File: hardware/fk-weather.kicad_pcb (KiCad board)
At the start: 2 copper layers, 28.7 x 107.4 mm, 78 parts, among them J1 MICRO-USB, J2 CONN_01X03, J6 CONN-HDR-2x5, M1 MOUNT_HOLE, M2 MOUNT_HOLE, M3 MOUNT_HOLE, M4 MOUNT_HOLE, P101 CONN_01X05, Q1 2N7002LT1G, Q2 2N7002LT1G, Q3 2N7002LT1G, SW1 SPNO, U1 ATSAMD21G18A-AU, U101 TSL2591, U102 MPL3115A2, U103 BNO055, U104 SHT31, U2 MCP1700T-XXX2E, U3 MAX4466, Y1 FC-135, Y101 FC-135

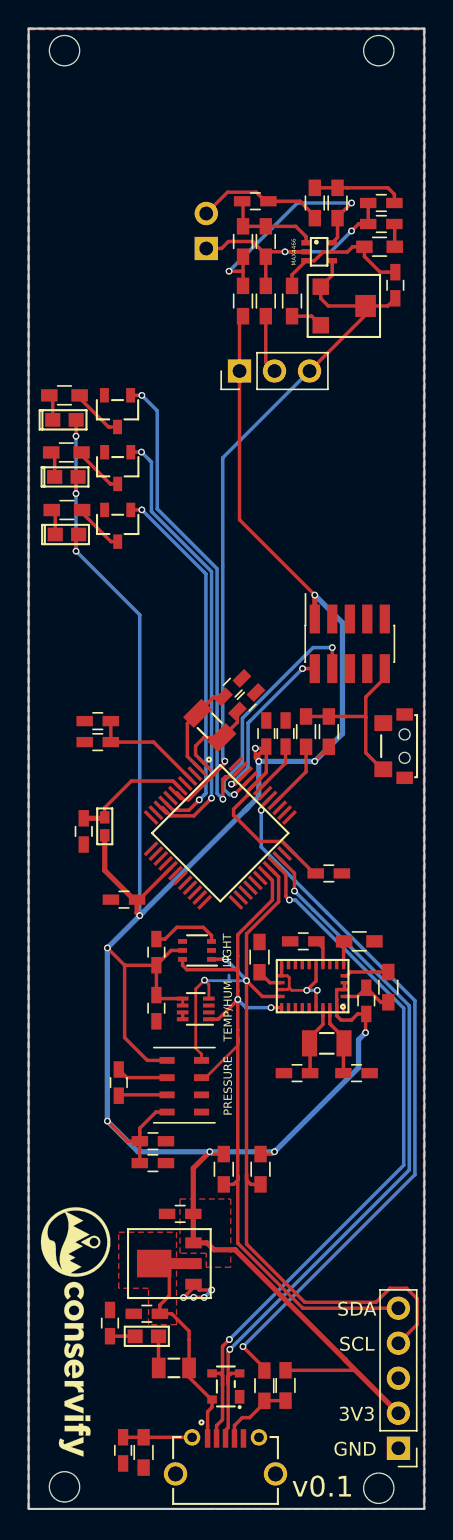
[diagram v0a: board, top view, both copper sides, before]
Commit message: Working on layout issues, trying to figure out the MCU problem.
Also broke up power from USB.
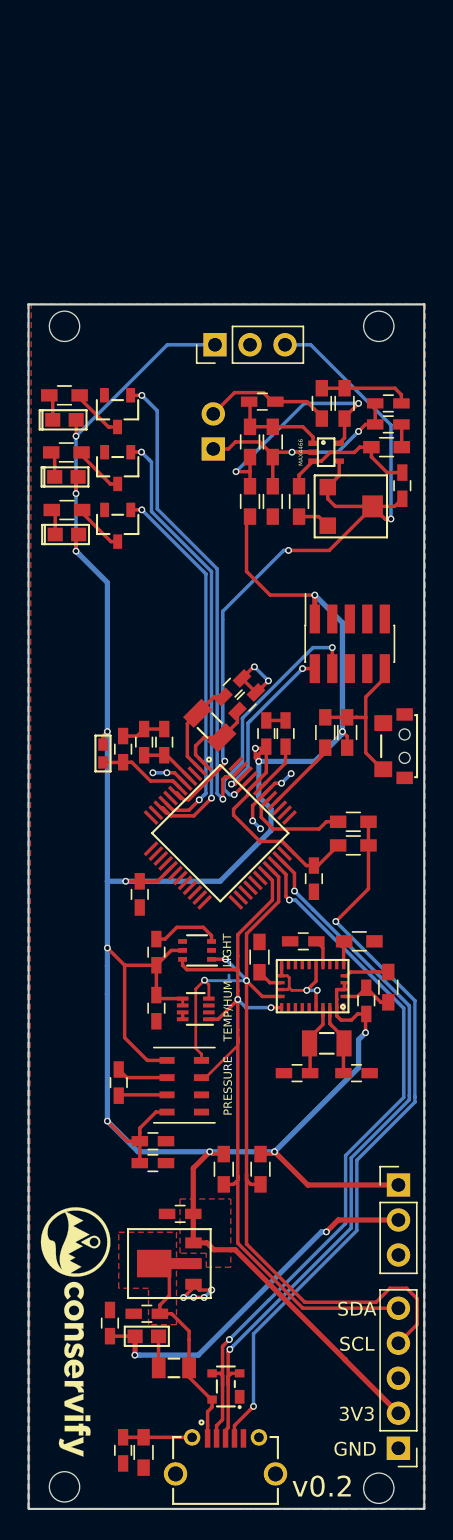
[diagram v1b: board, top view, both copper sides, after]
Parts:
- added J3: CONN_01X03, Socket_Strips:Socket_Strip_Straight_1x03_Pitch2.54mm, F.Cu at (152.6, 131.7)
- moved R9 41.4 mm to (149.4, 105.3), turned to 180 degrees
- moved R8 39.5 mm to (149.4, 107.1), turned to 0 degrees
- moved M3 20.0 mm to (128.4, 69.4)
- moved M4 20.0 mm to (151.2, 69.4)
- moved L3 14.6 mm to (141.9, 82.1)
- moved L4 14.6 mm to (143.5, 82.1)
- moved R16 14.6 mm to (145.4, 82.1)
- moved MK1 14.6 mm to (139.2, 78.3)
- moved C13 14.6 mm to (151.9, 75.0)
- moved C15 14.6 mm to (142.7, 74.9)
- moved C16 14.6 mm to (151.9, 76.5)
- moved C17 14.6 mm to (152.9, 81.0)
- moved R11 14.6 mm to (148.7, 75.0)
- moved R12 14.6 mm to (147.1, 75.0)
- moved RV1 14.6 mm to (149.3, 82.5)
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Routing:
- net Net-(J1-Pad4): track 5.48 -> 53.5 mm, vias 0 -> 2
- net /USB_ID: track 52.2 -> 7.80 mm, vias 2 -> 0
- net 5V0: track 1.81 -> 26.4 mm, vias 0 -> 2
- net GND: track 30.7 -> 44.8 mm, vias 6 -> 14
- net /A1: track 51.4 -> 58.2 mm, vias 1 -> 3
- net AREF: track 8.37 -> 4.03 mm
- net 3V3: track 241.2 -> 244.0 mm, vias 13 -> 14
- net Net-(C4-Pad1): track 8.76 -> 6.40 mm
- net /RST: track 13.0 -> 11.4 mm
- net /RESET: track 5.01 -> 5.76 mm
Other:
- board size 28.7 x 107.4 mm -> 28.7 x 87.4 mm
- board text added: "v0.2"
- board text removed: "v0.1"

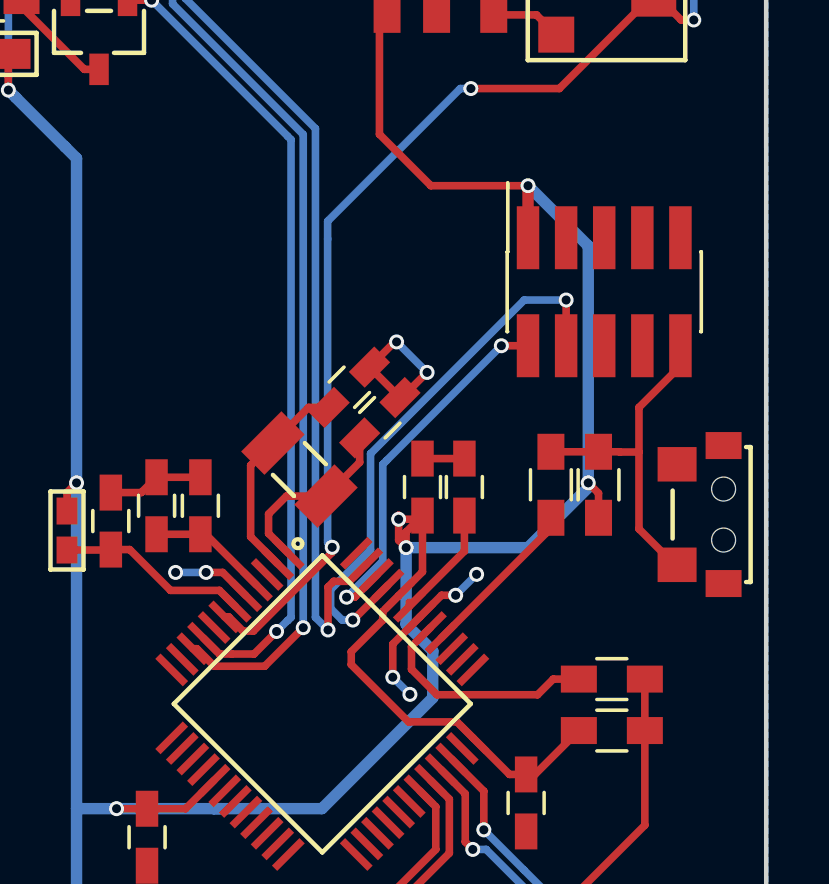
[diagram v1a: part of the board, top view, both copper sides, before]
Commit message: Programming header was wrong from the SMD switch.
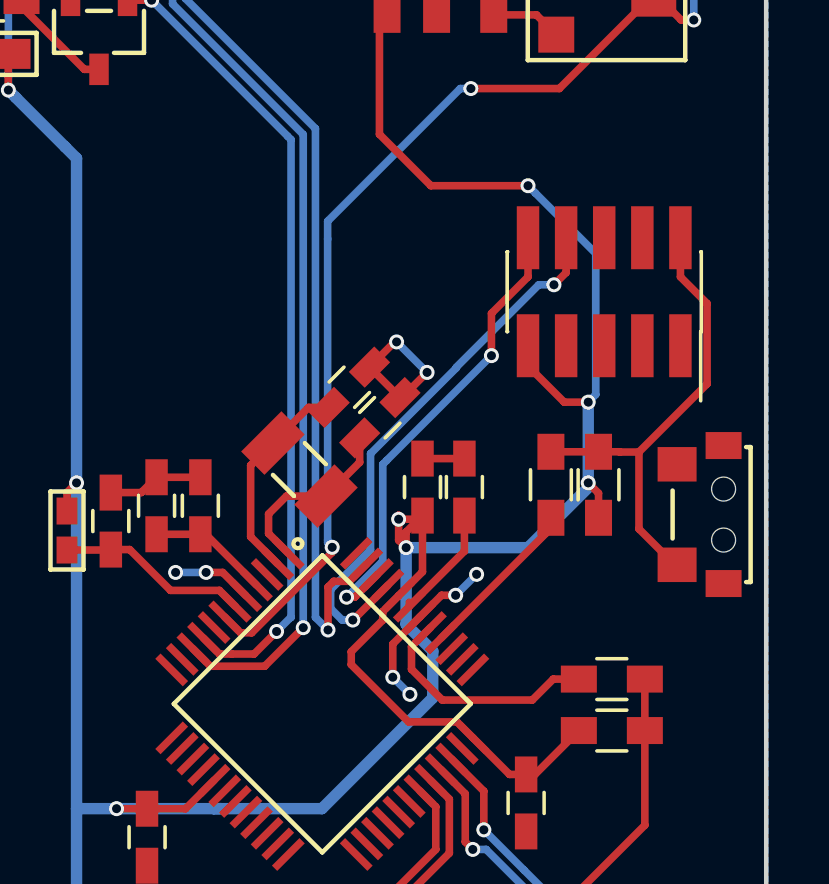
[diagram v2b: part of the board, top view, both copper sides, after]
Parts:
- turned J6 to 270 degrees
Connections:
- J6 pad 1: 3V3 -> GND
- J6 pad 10: /RST -> /SWDIO
- J6 pad 2: /SWDIO -> /RST
- J6 pad 3: GND -> Net-(J6-Pad3)
- J6 pad 4: /SWCLK -> Net-(J6-Pad4)
- J6 pad 7: Net-(J6-Pad7) -> GND
- J6 pad 8: Net-(J6-Pad8) -> /SWCLK
- J6 pad 9: GND -> 3V3
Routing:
- net /RST: track 11.4 -> 15.7 mm
- net /SWDIO: track 12.8 -> 15.9 mm
- net 3V3: track 244.0 -> 245.6 mm, vias 14 -> 15
- net GND: track 44.8 -> 45.4 mm

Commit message: Adding an LED to D13
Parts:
- added D5: Orange, RocketScreamKicadLibrary:LED-0603, F.Cu at (152.3, 106.5)
- added Q4: 2N7002LT1G, RocketScreamKicadLibrary:SOT-23, F.Cu at (152.4, 110.9)
- added R17: 2k2, Resistors_SMD:R_0603_HandSoldering, F.Cu at (152.4, 108.1)
- moved R8 2.32 mm to (148.4, 104.9)
- moved R9 2.15 mm to (148.4, 103.4)
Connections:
- U1 pad 26: Net-(U1-Pad26) -> /D13
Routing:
- net /D13: track 0.00 -> 12.8 mm, vias 0 -> 2
- net 3V3: track 245.6 -> 252.7 mm
- net Net-(Q4-Pad3): track 0.00 -> 2.15 mm
- net Net-(D5-Pad1): track 0.00 -> 1.79 mm
- net Net-(J1-Pad4): track 53.5 -> 55.1 mm

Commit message: Removing extraneous headers.
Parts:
- removed P101: CONN_01X05, Socket_Strips:Socket_Strip_Straight_1x05_Pitch2.54mm
- J3: value CONN_01X03 -> CONN_01X06; footprint Socket_Strips:Socket_Strip_Straight_1x03_Pitch2.54mm -> Socket_Strips:Socket_Strip_Straight_1x06_Pitch2.54mm
- moved J3 19.1 mm to (152.6, 150.8), turned to 180 degrees
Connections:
- J3 pad 1: 3V3 -> GND
- J3 pad 2: 5V0 -> 3V3
- J3 pad 3: GND -> Net-(J3-Pad3)
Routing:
- net 3V3: track 252.7 -> 241.9 mm
- net 5V0: track 26.4 -> 25.0 mm
- net /SCL: track 66.1 -> 65.2 mm

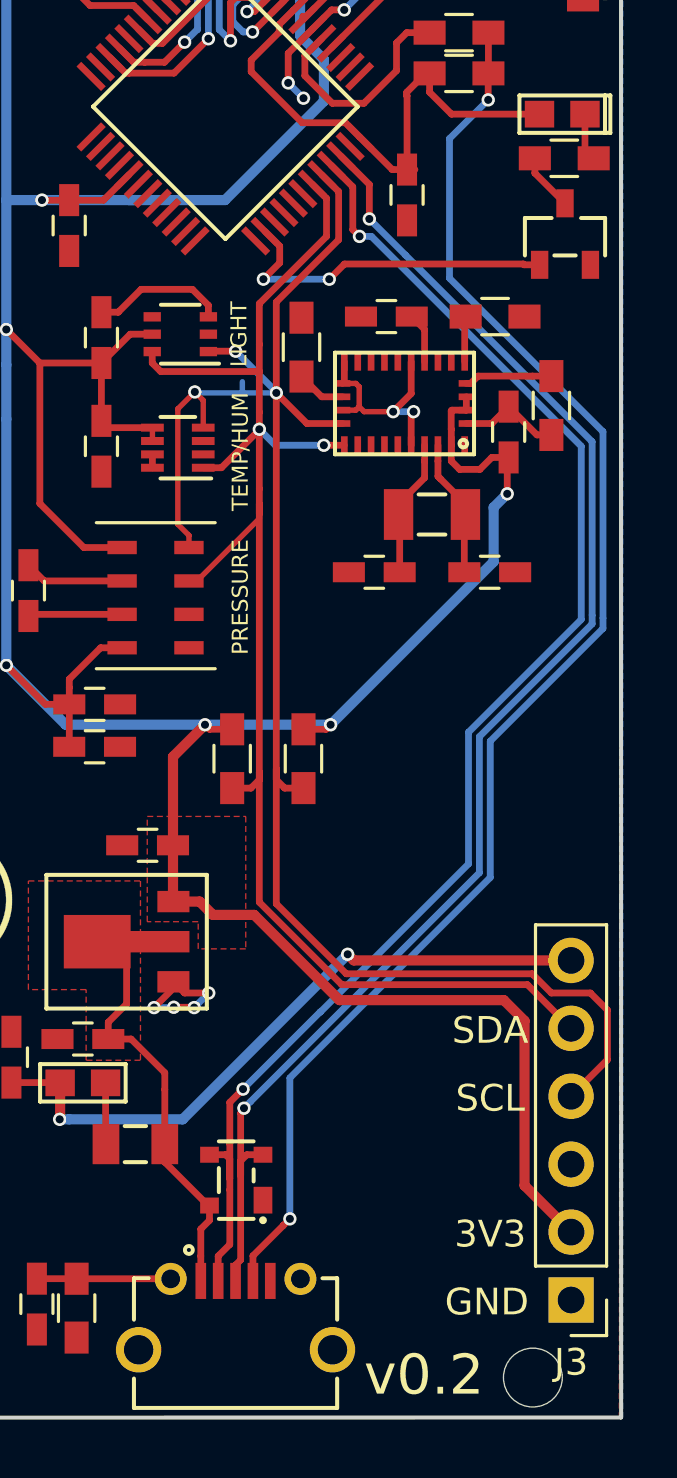
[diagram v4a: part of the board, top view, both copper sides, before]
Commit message: Adding a header for an LED.
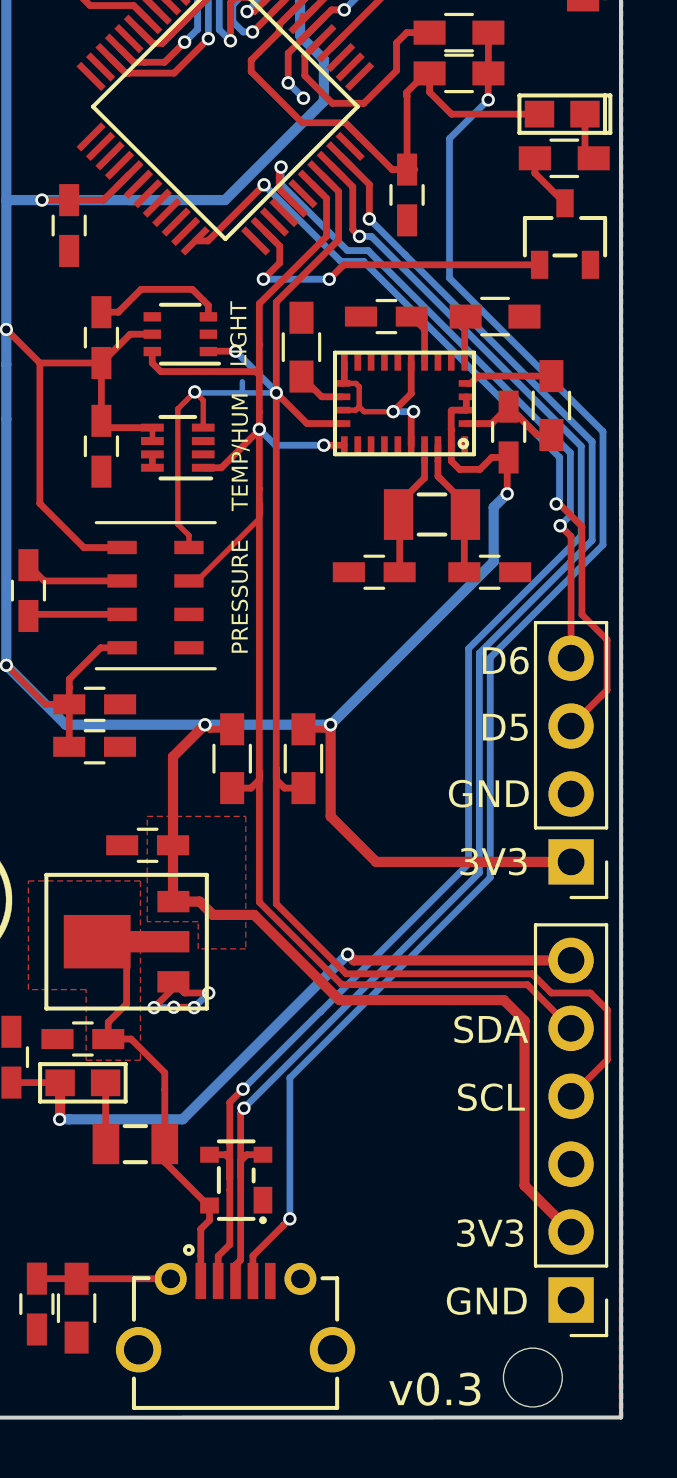
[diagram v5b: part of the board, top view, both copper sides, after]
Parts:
- added J4: CONN_01X04, Socket_Strips:Socket_Strip_Straight_1x04_Pitch2.54mm, F.Cu at (152.6, 134.4)
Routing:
- net /D5: track 0.00 -> 30.3 mm, vias 0 -> 2
- net /D6: track 0.00 -> 25.2 mm, vias 0 -> 2
- net 3V3: track 241.9 -> 255.1 mm
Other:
- board text added: "D5"
- board text added: "D6"
- board text added: "v0.3"
- board text removed: "v0.2"

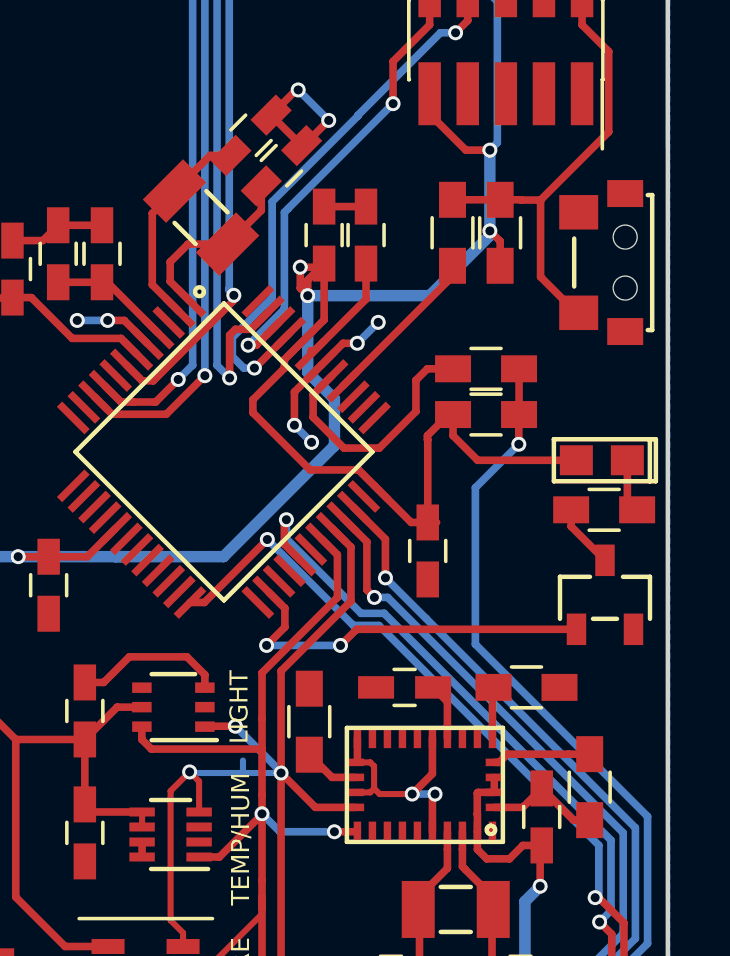
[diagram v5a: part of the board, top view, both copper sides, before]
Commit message: Nudge button over.
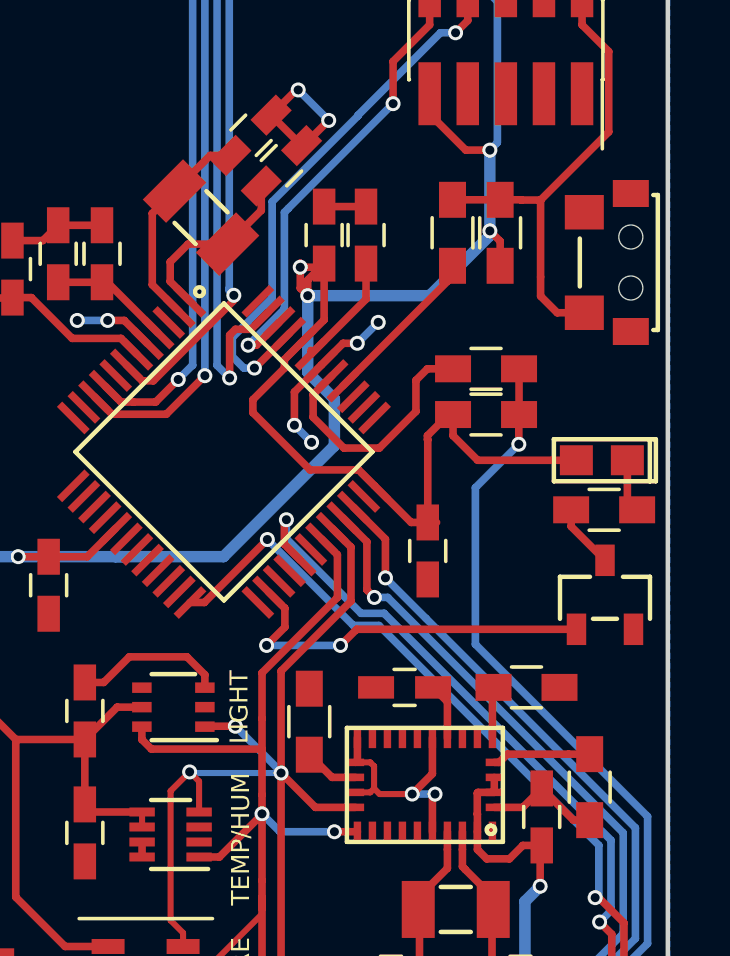
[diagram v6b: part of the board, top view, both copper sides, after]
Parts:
- moved SW1 0.19 mm to (153.5, 99.9)
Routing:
- net /RST: track 15.7 -> 16.3 mm
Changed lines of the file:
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@@
   (general
     (links 180)
-    (no_connects 41)
+    (no_connects 0)
     (area 106.352905 47.75 165.914286 159.377948)
     (thickness 1.6)
@@
   )
   (module RocketScreamKicadLibrary:TS-018 (layer F.Cu)
-    (at 153.2763 99.861 270)
+    (at 153.4636 99.8592 270)
     (tags SPST)
     (fp_text reference SW1 (at 0 -3.175 270) (layer F.SilkS) hide
@@
   (segment (start 140.726233 103.378) (end 141.892031 102.212202) (width 0.254) (layer F.Cu) (net 13))
   (via (at 140.716 103.378) (size 0.5) (drill 0.3) (layers F.Cu B.Cu) (net 13))
+  (segment (start 151.7136 101.5342) (end 150.8096 101.5342) (width 0.254) (layer F.Cu) (net 15))
+  (segment (start 150.8096 101.5342) (end 150.2556 100.9802) (width 0.254) (layer F.Cu) (net 15))
+  (segment (start 150.2556 100.9802) (end 150.2556 100.3403) (width 0.254) (layer F.Cu) (net 15))
   (segment (start 152.527 95.5059) (end 152.527 92.827) (width 0.254) (layer F.Cu) (net 15))
   (segment (start 152.527 92.827) (end 151.638 91.938) (width 0.254) (layer F.Cu) (net 15))
@@
   (segment (start 147.32 97.7695) (end 148.9075 97.7695) (width 0.254) (layer F.Cu) (net 15))
   (segment (start 150.2556 97.7773) (end 150.2556 100.3403) (width 0.254) (layer F.Cu) (net 15))
-  (segment (start 150.2556 100.3403) (end 151.4513 101.536) (width 0.254) (layer F.Cu) (net 15))
-  (segment (start 151.4513 101.536) (end 151.5263 101.536) (width 0.254) (layer F.Cu) (net 15))
   (segment (start 141.605 130.937) (end 141.605 135.984196) (width 0.254) (layer F.Cu) (net 16))
   (segment (start 141.605 135.984196) (end 144.2212 138.600396) (width 0.254) (layer F.Cu) (net 16))
@@
   (segment (start 140.335 116.876426) (end 138.593426 116.876426) (width 0.2032) (layer B.Cu) (net 16))
   (segment (start 141.605 116.876426) (end 140.335 116.876426) (width 0.2032) (layer B.Cu) (net 16))
-  (segment (start 140.335 116.876426) (end 140.335 116.459) (width 0.2032) (layer B.Cu) (net 16))
   (segment (start 138.872 118.17553) (end 138.872 117.155) (width 0.2032) (layer F.Cu) (net 16))
   (segment (start 138.872 117.155) (end 138.557 116.84) (width 0.2032) (layer F.Cu) (net 16))

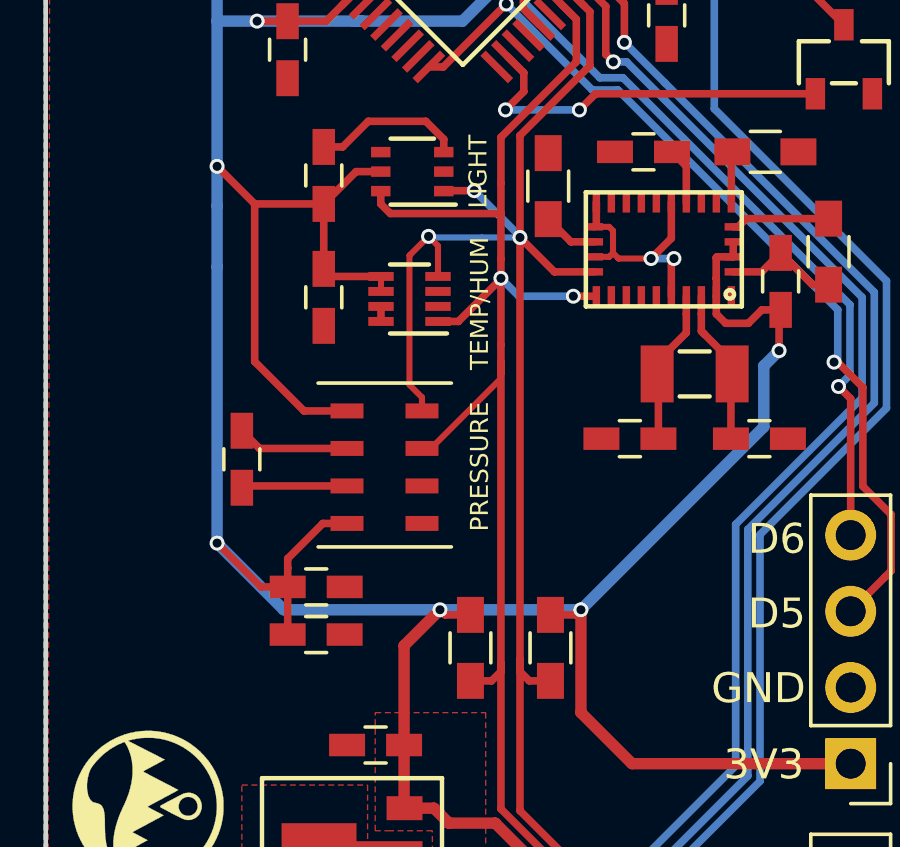
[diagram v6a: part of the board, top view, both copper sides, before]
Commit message: Wire ADDR on SHT31 to GND.
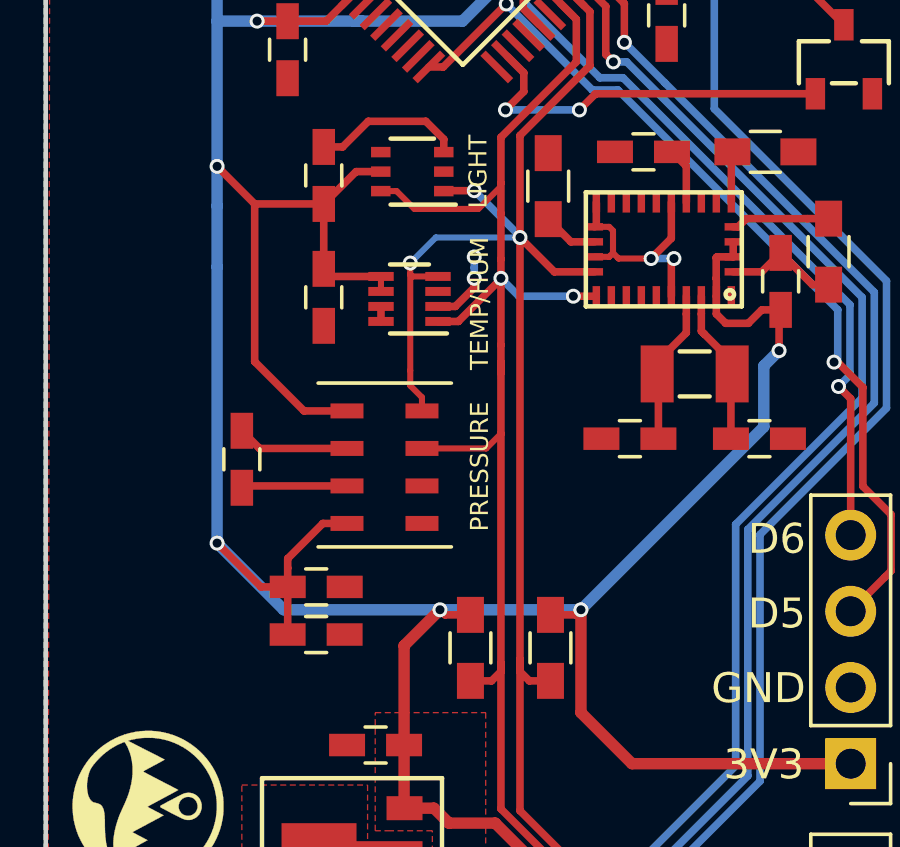
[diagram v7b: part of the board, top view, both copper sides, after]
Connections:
- U104 pad 2: Net-(U104-Pad2) -> GND
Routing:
- net GND: track 45.4 -> 47.9 mm, vias 14 -> 16
- net /SCL: track 64.8 -> 64.1 mm
